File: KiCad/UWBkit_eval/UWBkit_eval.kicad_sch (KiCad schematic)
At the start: 0 parts

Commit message: Added RF module to schematic
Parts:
- added C1, C2: 330p, symbol Device:C_Small
- added C3: 100n, symbol Device:C_Small
- added C4: 10u, symbol Device:C_Polarized_Small
- added D1: G, symbol Device:LED_Small
- added D2: B, symbol Device:LED_Small
- added D3, D4: R, symbol Device:LED_Small
- added D5: LED_Dual_AAKK, symbol Device:LED_Dual_AAKK
- added Q1, Q2: Q_NMOS_DGS, symbol Transistor_FET:Q_NMOS_DGS
- added R1, R2, R3, R4: 1k8, symbol Device:R_Small
- added R10, R5, R7, R8, R9: 150R, symbol Device:R_Small
- added R6: 820R, symbol Device:R_Small
- added SW1, SW2: SW_Push, symbol Switch:SW_Push
- added U1: DWM3001C, DWM3001C:XCVR_DWM3001C, symbol DWM3001C:DWM3001C
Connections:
- new net: Q1.2 (G), R10.1, R8.2
- new net: D5.1 (A1), R6.2
- new net: D3.1 (K), R2.1
- new net: Q2.2 (G), R7.2, R9.1
- new net: D5.4 (K2), Q2.1 (D)
- new net: D5.2 (A2), R5.2
- new net: D4.1 (K), R1.1
- new net: D5.3 (K1), Q1.1 (D)
- new net: D2.1 (K), R3.1
- new net: D1.1 (K), R4.1
- new net: R4.2, U1.10 (P0.04)
- new net: R3.2, U1.9 (P0.05)
- new net: R1.2, U1.7 (P0.14)
- new net: R2.2, U1.8 (P0.22)
- new net +3V3: C3.1, C4.1, D1.2 (A), D2.2 (A), D3.2 (A), D4.2 (A), R5.1, R6.1, U1.12 (VDD)
- new net CS_RPI: U1.43 (P0.30)
- new net DW_GP0: U1.36 (DW_GP0)
- new net DW_GP1: U1.35 (DW_GP1)
- new net DW_GP5: U1.30 (DW_GP5)
- new net DW_GP6: U1.31 (DW_GP6)
- new net GND: C1.1, C2.1, C3.2, C4.2, Q1.3 (S), Q2.3 (S), R10.2, R9.2, SW1.1, SW2.1, U1.1 (GND), U1.11 (GND), U1.21 (GND), U1.38 (GND), U1.48 (GND)
- new net IO_13: U1.13 (P0.12)
- new net IO_16: U1.16 (P0.21)
- new net IO_17: U1.17 (P0.20)
- new net IO_24: U1.24 (P0.06)
- new net IO_25: U1.25 (P1.01)
- new net IO_26: U1.26 (P0.13)
- new net IO_27: U1.27 (P1.09)
- new net IO_28: U1.28 (P1.00)
- new net IO_29: U1.29 (P1.05)
- new net IO_6: U1.6 (P0.17)
- new net IO_RPI: U1.33 (P0.28)
- new net NF1: C2.2, U1.4 (P0.10/NFC2)
- new net NF2: C1.2, U1.5 (P0.09/NFC1)
- new net NRF_D+: U1.20 (USB_P)
- new net NRF_D-: U1.19 (USB_N)
- new net NRF_VBUS: U1.18 (VUSB)
- new net RESET: SW1.2, U1.47 (~{RESET}/P0.18)
- new net RXD: U1.34 (P0.19)
- new net RX_LED: R8.1, U1.45 (DW_GP2)
- new net SCL: U1.15 (I2C0_SCL)
- new net SCL_RPI: U1.39 (P0.23)
- new net SDA: U1.14 (I2C0_SDA)
- new net SDA_RPI: U1.37 (P0.26)
- new net SPI_CLK: U1.42 (P0.31)
- new net SPI_MISO: U1.40 (P0.07)
- new net SPI_MOSI: U1.41 (P0.27)
- new net SW2: SW2.2, U1.46 (P0.02)
- new net SWCLK: U1.2 (SWD_CLK)
- new net SWDIO: U1.3 (SWD_DIO)
- new net TXD: U1.32 (P0.15)
- new net TX_LED: R7.1, U1.44 (DW_GP3)

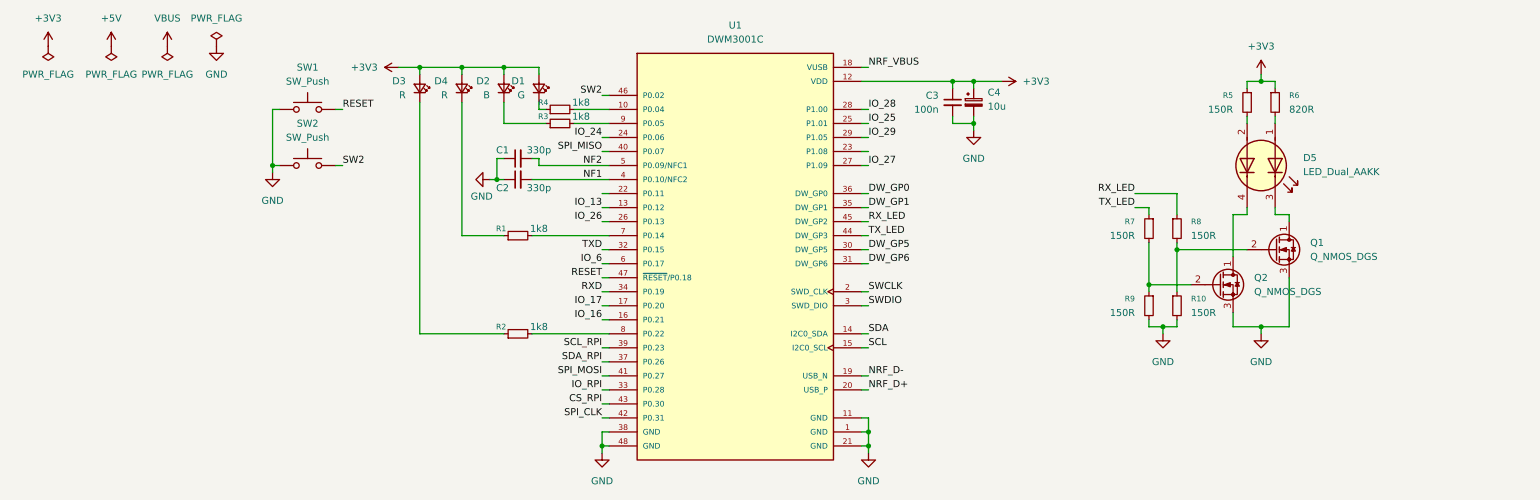
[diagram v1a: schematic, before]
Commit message: Added usb port
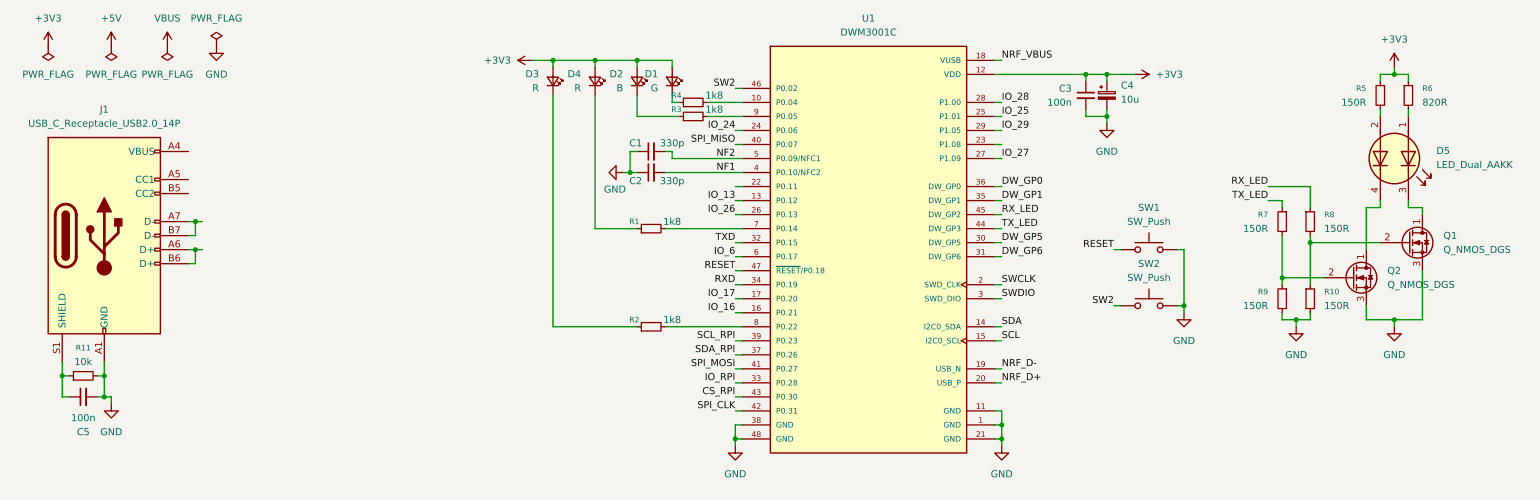
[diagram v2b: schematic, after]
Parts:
- added C5: 100n, symbol Device:C_Small
- added J1: USB_C_Receptacle_USB2.0_14P, symbol Connector:USB_C_Receptacle_USB2.0_14P
- added R11: 10k, symbol Device:R_Small
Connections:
- net GND: now also C5.2, J1.A1 (GND), J1.A12 (GND), J1.B1 (GND), J1.B12 (GND), R11.2
- new net: C5.1, J1.S1 (SHIELD), R11.1
- new net: J1.A4 (VBUS), J1.A9 (VBUS), J1.B4 (VBUS), J1.B9 (VBUS)
- new net: J1.A6 (D+), J1.B6 (D+)
- new net: J1.A7 (D-), J1.B7 (D-)
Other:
- moved on the sheet: C1, C2, C3, C4, D1, D2, D3, D4, D5, Q1, Q2, R1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

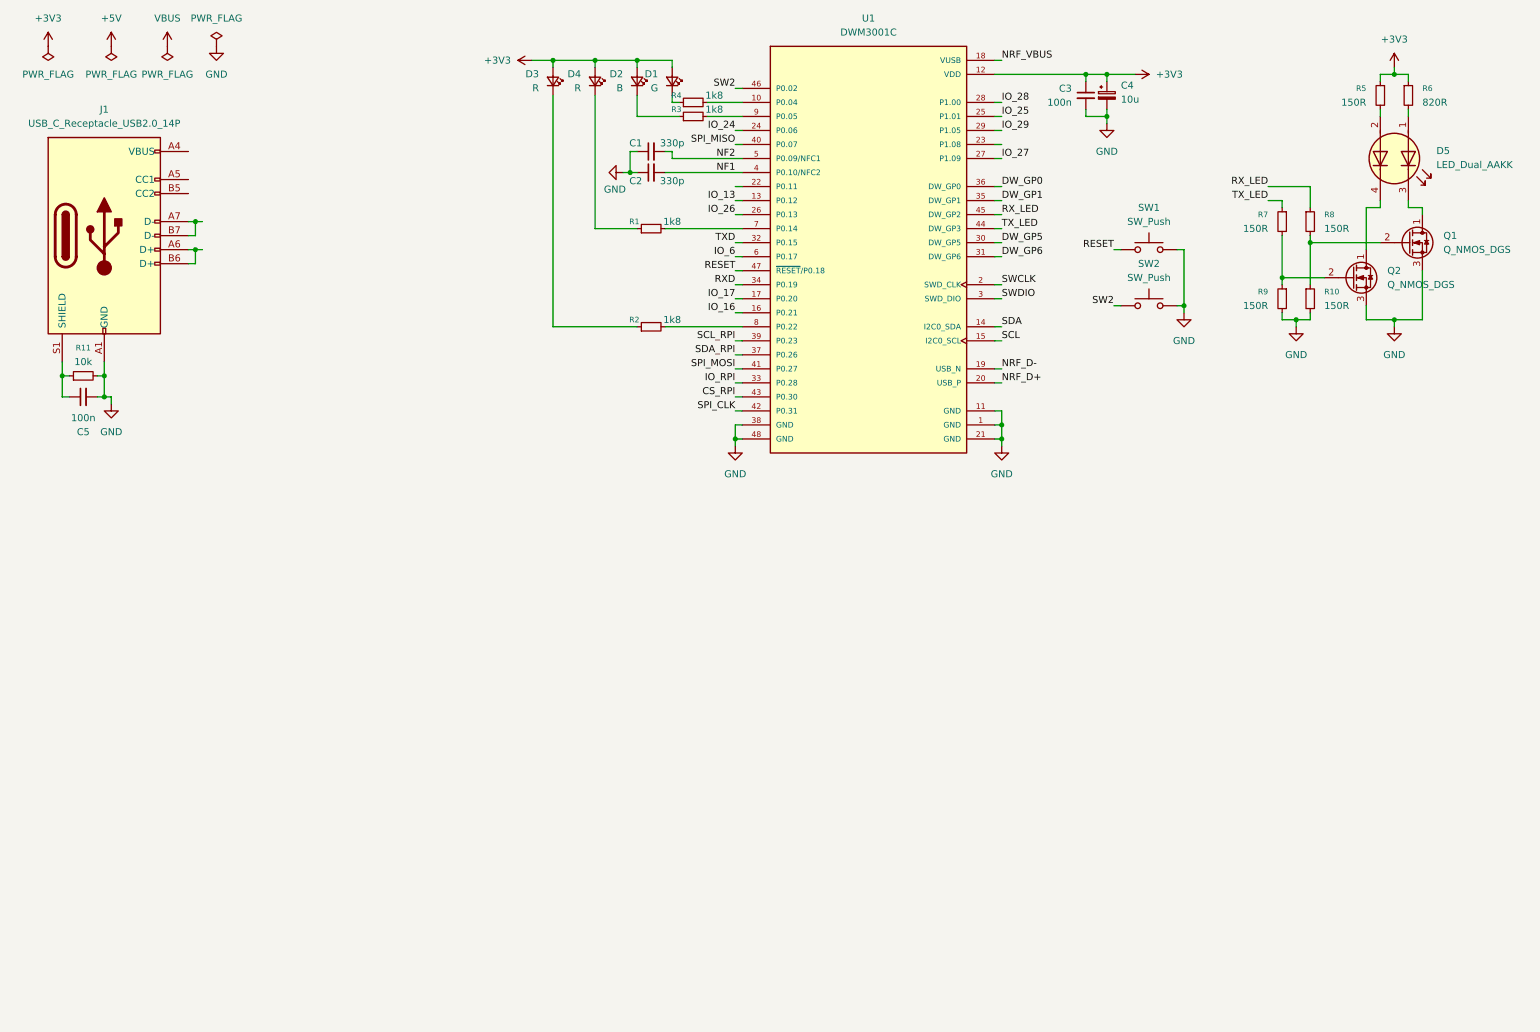
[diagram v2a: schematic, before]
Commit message: Added connectors
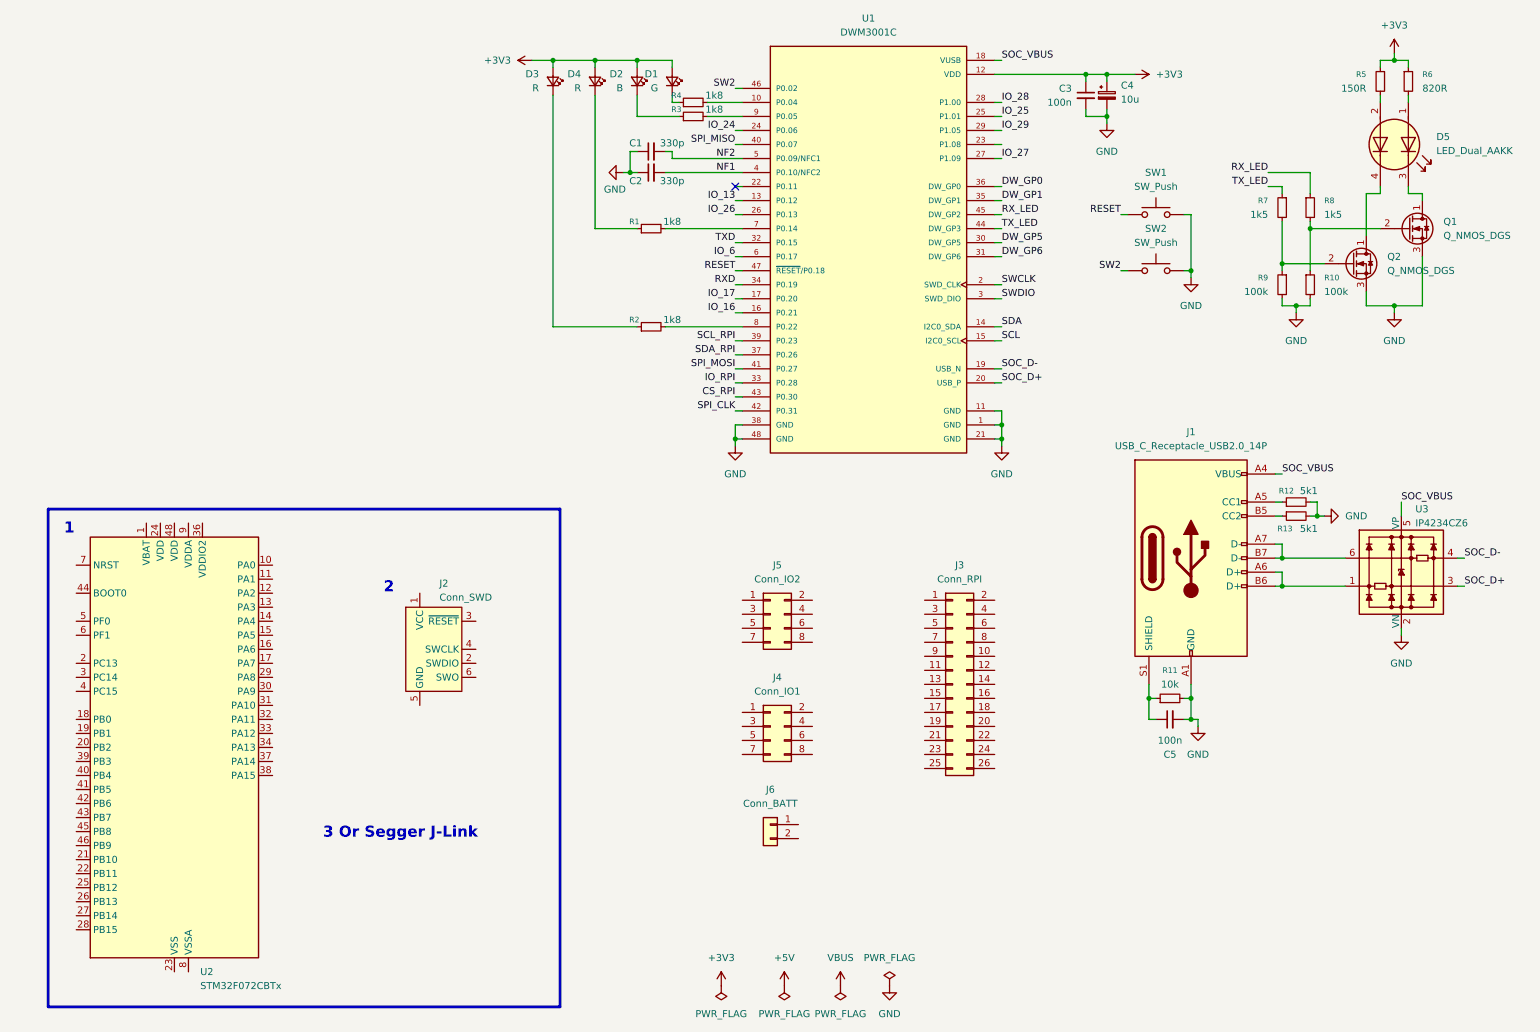
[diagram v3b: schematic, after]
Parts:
- added J2: Conn_SWD, Connector:Tag-Connect_TC2030-IDC-FP_2x03_P1.27mm_Vertical, symbol Connector:Conn_ARM_SWD_TagConnect_TC2030
- added J3: Conn_RPI, symbol Connector_Generic:Conn_02x13_Odd_Even
- added J4: Conn_IO1, symbol Connector_Generic:Conn_02x04_Odd_Even
- added J5: Conn_IO2, symbol Connector_Generic:Conn_02x04_Odd_Even
- added J6: Conn_BATT, symbol Connector_Generic:Conn_01x02
- added R12, R13: 5k1, symbol Device:R_Small
- added U2: STM32F072CBTx, Package_QFP:LQFP-48_7x7mm_P0.5mm, symbol MCU_ST_STM32F0:STM32F072CBTx
- added U3: IP4234CZ6, Package_TO_SOT_SMD:SC-74-6_1.55x2.9mm_P0.95mm, symbol Power_Protection:IP4234CZ6
- R10, R9: value 150R -> 100k
- R7, R8: value 150R -> 1k5
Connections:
- net NRF_VBUS is gone; now on net SOC_VBUS: U1.18 (VUSB)
- net GND: now also R12.2, R13.2, U3.2 (VN)
- net SOC_VBUS: now reaches J1.A4 (VBUS), J1.A9 (VBUS), J1.B4 (VBUS), J1.B9 (VBUS)
- net SOC_VBUS: now also U3.5 (VP)
- net at J1.A5 (CC1): now also R12.1
- net at J1.A6 (D+), J1.B6 (D+): now also U3.1
- net at J1.A7 (D-), J1.B7 (D-): now also U3.6
- net at J1.B5 (CC2): now also R13.1
- net NRF_D+ renamed SOC_D+
- net SOC_D+: now also U3.3
- net NRF_D- renamed SOC_D-
- net SOC_D-: now also U3.4
- new net: U2.23 (VSS), U2.35 (VSS), U2.47 (VSS)
- no-connect marks 0 -> 1
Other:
- note added: "1"
- note added: "2"
- note added: "3 Or Segger J-Link"
- moved on the sheet: C5, D5, J1, Q1, Q2, R10, R11, R5, R6, R7, R8, R9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

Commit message: Assigned pins to connectors, added battery protection, edited LED footprint
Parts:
- removed D5: LED_Dual_AAKK, symbol Device:LED_Dual_AAKK
- added C6: 100n, symbol Device:C_Small
- added C7, C9: 10u, symbol Device:C_Polarized_Small
- added D10, D6: PESD5V2S2UT, symbol Device:D_Zener_Dual_CommonAnode_KKA
- added D7: LSG T676, symbol LED_Dual:LED_Dual_KAKA_RG
- added J7: Conn_SWD, Connector:Tag-Connect_TC2030-IDC-FP_2x03_P1.27mm_Vertical, symbol Connector:Conn_ARM_SWD_TagConnect_TC2030
- added L1: 2.2u, symbol Device:L_Small
- added Q3: Q_PMOS, symbol Device:Q_PMOS
- added R14: 100k, symbol Device:R_Small
- added R15: 220R, symbol Device:R_Small
- added U4: eFuse, Package_TO_SOT_SMD:TSOT-23, symbol Regulator_Linear:AP2127N3-1.2
- added U5: MAX40203AUK+T, Package_TO_SOT_SMD:SOT-23-5, symbol Ideal_Diode:MAX40203AUK+T
- added U6: XC9285B33CMR-G, Package_TO_SOT_SMD:SOT-23-5, symbol DCDC_Converter_Custom:XC9285B33CMR-G
- J4: value Conn_IO1 -> Conn_IO2
- J5: value Conn_IO2 -> Conn_IO1
- R6: value 820R -> 330R
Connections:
- net +3V3: now also J2.1 (VCC), C9.1, L1.2, R15.1, U6.4 (VOUT)
- net CS_RPI: now also J3.24 (Pin_24)
- net DW_GP0: now also J4.2 (Pin_2)
- net DW_GP1: now also J4.1 (Pin_1)
- net DW_GP5: now also J5.1 (Pin_1)
- net DW_GP6: now also J5.2 (Pin_2)
- net GND: now also J2.5 (GND), J3.14 (Pin_14), J3.20 (Pin_20), J3.25 (Pin_25), J3.6 (Pin_6), J3.9 (Pin_9), J6.2 (Pin_2), C6.2, C7.2, C9.2, D10.1 (K), D6.1 (K), R14.2, U5.2 (GND), U6.2 (GND)
- net IO_13: now also J4.4 (Pin_4)
- net IO_16: now also J4.7 (Pin_7)
- net IO_17: now also J4.8 (Pin_8)
- net IO_24: now also J5.7 (Pin_7)
- net IO_25: now also J5.8 (Pin_8)
- net IO_26: now also J5.5 (Pin_5)
- net IO_27: now also J5.6 (Pin_6)
- net IO_28: now also J5.3 (Pin_3)
- net IO_29: now also J5.4 (Pin_4)
- net IO_6: now also J4.3 (Pin_3)
- net IO_RPI: now also J3.15 (Pin_15)
- net RESET: now also J2.3 (~{RESET}), J3.12 (Pin_12)
- net RXD: now also J3.10 (Pin_10)
- net SCL: now also J4.6 (Pin_6)
- net SCL_RPI: now also J3.5 (Pin_5)
- net SDA: now also J4.5 (Pin_5)
- net SDA_RPI: now also J3.3 (Pin_3)
- net SOC_VBUS: now also J3.2 (Pin_2), J3.4 (Pin_4), D10.2 (K), D6.2 (K), Q3.G, R14.1, U5.1 (VDD), U5.3 (EN)
- net SPI_CLK: now also J3.23 (Pin_23)
- net SPI_MISO: now also J3.21 (Pin_21)
- net SPI_MOSI: now also J3.19 (Pin_19)
- net SWCLK: now also J2.4 (SWCLK)
- net SWDIO: now also J2.2 (SWDIO)
- net TXD: now also J3.8 (Pin_8)
- net at R6.2: now also D7.4 (A2), R15.2
- net V_BATT: now reaches J6.1 (Pin_1)
- net V_BATT: now also Q3.D
- net at Q2.1 (D): now also D7.1 (K1)
- net at R5.2: now also D7.2 (A1)
- net at Q1.1 (D): now also D7.3 (K2)
- new net: C6.1, C7.1, Q3.S, U5.5 (OUT), U6.1 (VIN), U6.3 (EN)
- new net: L1.1, U6.5 (Lx)
- no-connect marks 1 -> 13
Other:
- note added: "Battery shutoff"
- moved on the sheet: C1, C2, C3, C4, C5, D1, D2, D3, D4, J1, J2, J3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

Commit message: First version of the board
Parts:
- removed C1, C2: 330p, symbol Device:C_Small
- removed Q1, Q2: Q_NMOS_DGS, symbol Transistor_FET:Q_NMOS_DGS
- removed Q3: Q_PMOS, symbol Device:Q_PMOS
- removed R7, R8: 1k5, symbol Device:R_Small
- added H1, H2, H3, H4: MountingHole_Pad, MountingHole:MountingHole_3.2mm_M3_ISO14580_Pad_TopBottom, symbol Mechanical:MountingHole_Pad
- added Q1: BSS341, Package_TO_SOT_SMD:SOT-23-3, symbol Transistor_FET:BSS84
- added Q2, Q3: BSS138, Package_TO_SOT_SMD:SOT-23, symbol Transistor_FET:BSS138
- C1: renamed from C3; footprint (none) -> Capacitor_SMD:C_0603_1608Metric
- C2: renamed from C4; footprint (none) -> Capacitor_Tantalum_SMD:CP_EIA-3216-18_Kemet-A
- C3: renamed from C6; footprint (none) -> Capacitor_SMD:C_0603_1608Metric
- C4: renamed from C7; footprint (none) -> Capacitor_Tantalum_SMD:CP_EIA-3216-18_Kemet-A
- C5: renamed from C9; footprint (none) -> Capacitor_Tantalum_SMD:CP_EIA-3216-18_Kemet-A
- C6: renamed from C5; footprint (none) -> Capacitor_SMD:C_0603_1608Metric
- D1: renamed from D3; footprint (none) -> LED_SMD:LED_0603_1608Metric
- D2: renamed from D4; footprint (none) -> LED_SMD:LED_0603_1608Metric
- D3: renamed from D2; footprint (none) -> LED_SMD:LED_0603_1608Metric
- D4: renamed from D1; footprint (none) -> LED_SMD:LED_0603_1608Metric
- D5: renamed from D7; footprint (none) -> LED_Dual:LED_Dual_OSRAM-PLCC4_3.2x2.8mm
- D6: renamed from D10; footprint (none) -> Package_TO_SOT_SMD:SOT-23
- D7: renamed from D6; footprint (none) -> Package_TO_SOT_SMD:SOT-23
- J2: renamed from J6; footprint (none) -> Connector_PinSocket_2.54mm:PinSocket_1x02_P2.54mm_Vertical
- J3: renamed from J4; footprint (none) -> Connector_PinHeader_2.54mm:PinHeader_2x04_P2.54mm_Vertical
- J4: renamed from J5; footprint (none) -> Connector_PinHeader_2.54mm:PinHeader_2x04_P2.54mm_Vertical
- J6: renamed from J3; footprint (none) -> Connector_PinSocket_2.54mm:PinSocket_2x13_P2.54mm_Vertical
- J7: renamed from J1; footprint (none) -> Connector_USB:USB_C_Receptacle_GCT_USB4105-xx-A_16P_TopMnt_Horizontal
- L1: footprint (none) -> Inductor_SMD:L_0805_2012Metric
- R1: renamed from R4; footprint (none) -> Resistor_SMD:R_0603_1608Metric
- R10, R9: value 100k -> 4k7; footprint (none) -> Resistor_SMD:R_0603_1608Metric
- R11: renamed from R12; footprint (none) -> Resistor_SMD:R_0603_1608Metric
- R12: renamed from R13; footprint (none) -> Resistor_SMD:R_0603_1608Metric
- R13: renamed from R11; footprint (none) -> Resistor_SMD:R_0603_1608Metric
- R2: renamed from R3; footprint (none) -> Resistor_SMD:R_0603_1608Metric
- R3: renamed from R5; footprint (none) -> Resistor_SMD:R_0603_1608Metric
- R4: renamed from R6; footprint (none) -> Resistor_SMD:R_0603_1608Metric
- R5: renamed from R15; footprint (none) -> Resistor_SMD:R_0603_1608Metric
- R6: renamed from R1; footprint (none) -> Resistor_SMD:R_0603_1608Metric
- R7: renamed from R14; footprint (none) -> Resistor_SMD:R_0603_1608Metric
- R8: renamed from R2; footprint (none) -> Resistor_SMD:R_0603_1608Metric
- SW1, SW2: footprint (none) -> Button_Switch_THT:SW_TH_Tactile_Omron_B3F-106x
- U3: renamed from U1; footprint DWM3001C:XCVR_DWM3001C -> UWBkit:DWM3001C
- renumbered J7 to J1, J2 to J5, U4 to U1, U5 to U2, U6 to U4, U2 to U5, U3 to U6
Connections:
- net +3V3: now also R10.2, R9.2
- net DW_GP0: now also J3.6 (Pin_6); no longer J3.2 (Pin_2)
- net DW_GP1: now also J3.8 (Pin_8); no longer J3.1 (Pin_1)
- net DW_GP5: now also J4.6 (Pin_6); no longer J4.1 (Pin_1)
- net DW_GP6: now also J4.8 (Pin_8); no longer J4.2 (Pin_2)
- net GND: now also H1.1, H2.1, H3.1, H4.1, Q2.2 (S), Q3.2 (S); no longer R10.2, R9.2
- net IO_16: now also J3.3 (Pin_3); no longer J3.7 (Pin_7)
- net IO_17: now also J3.1 (Pin_1); no longer J3.8 (Pin_8)
- net IO_25: now also J4.5 (Pin_5); no longer J4.8 (Pin_8)
- net IO_26: now also J4.3 (Pin_3); no longer J4.5 (Pin_5)
- net IO_27: now also J4.1 (Pin_1); no longer J4.6 (Pin_6)
- net IO_28: now also J4.2 (Pin_2); no longer J4.3 (Pin_3)
- net IO_6: now also J3.2 (Pin_2); no longer J3.3 (Pin_3)
- net RX_LED: now also Q2.1 (G)
- net SCL: now also J3.7 (Pin_7), R10.1; no longer J3.6 (Pin_6)
- net SDA: now also R9.1
- net SOC_VBUS: now also Q1.1 (G)
- net TX_LED: now also Q3.1 (G)
- net V_BATT: now also Q1.3 (D)
- net at C3.1, C4.1, U2.5 (OUT)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: now also Q1.2 (S)
- net at D5.1 (K1): now also Q3.3 (D)
- net at D5.3 (K2): now also Q2.3 (D)
- net NF1: no longer names the net of U3.4 (P0.10/NFC2)
- net NF2: no longer names the net of U3.5 (P0.09/NFC1)
- no-connect marks 13 -> 16
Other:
- moved on the sheet: J1, R7, U5
